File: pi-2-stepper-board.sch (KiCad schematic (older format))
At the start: 18 parts, among them CON1 DC12v, P1 Servo (A0), P2 Endstop1 (A1), P3 Endstop2 (A2), P4 Stepper1, P5 Stepper2, P6 COM, P7 Aux (D10 - 13), SW1 SW_PUSH, SW2 SPDT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

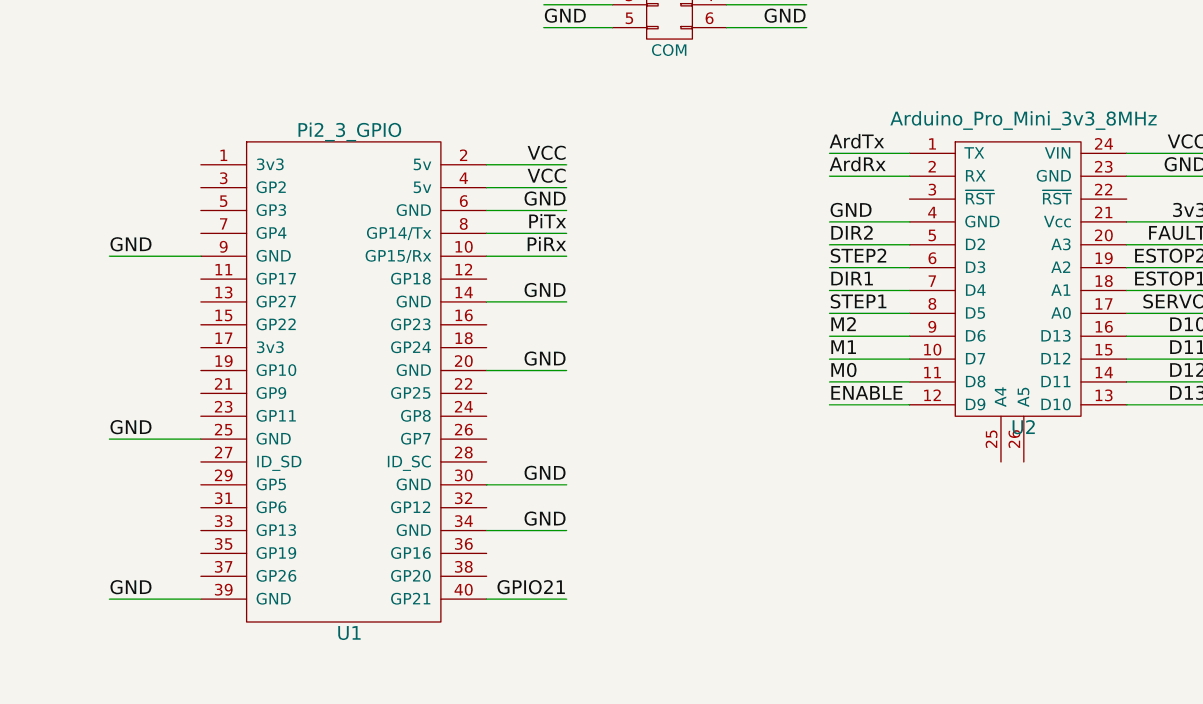
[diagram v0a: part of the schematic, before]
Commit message: Added I2C updated text
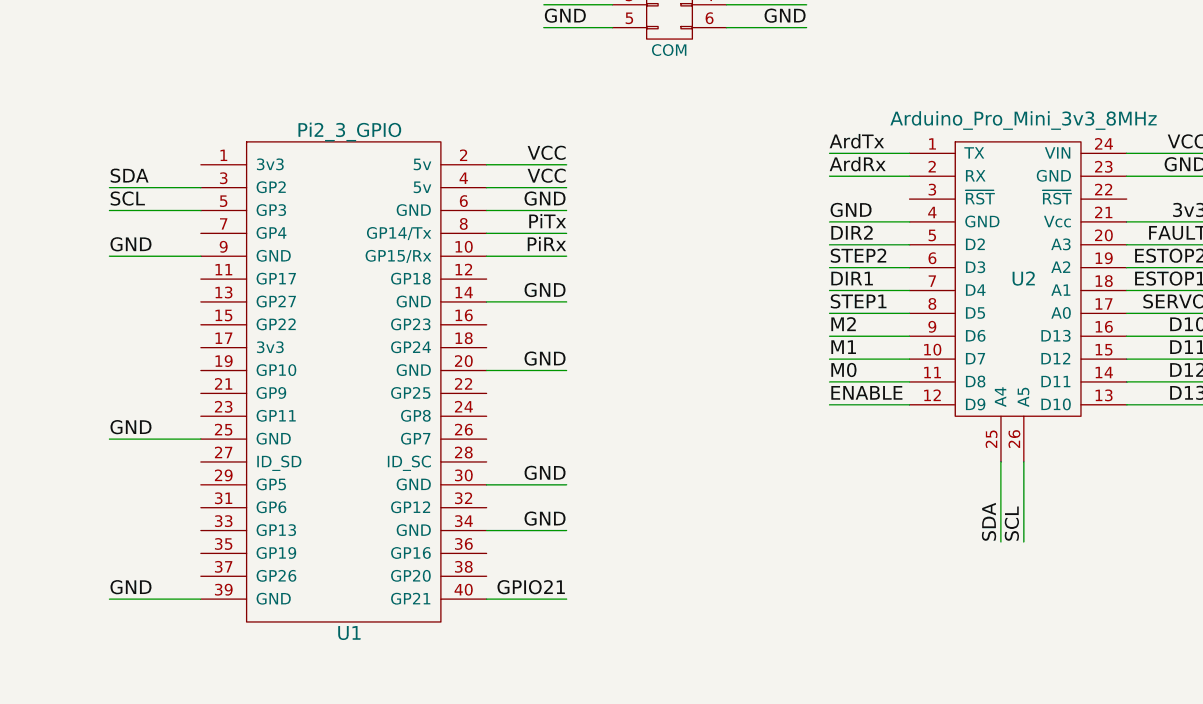
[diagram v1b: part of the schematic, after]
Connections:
- net SDA: now reaches U2.25 (A4)
- net SDA: now also U1.3 (GP2)
- net SCL: now reaches U2.26 (A5)
- net SCL: now also U1.5 (GP3)
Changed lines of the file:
@@
-$EndComp
-$Comp
-L Arduino_Pro_Mini_3v3_8MHz U2
-U 1 1 56E571C7
-P 5200 3050
-F 0 "U2" H 5200 2400 60  0000 C CNN
-F 1 "Arduino_Pro_Mini_3v3_8MHz" H 5200 3750 60  0000 C CNN
-F 2 "custom:Arduino_Pro_Mini" H 5200 2500 60  0001 C CNN
-F 3 "" H 5200 2500 60  0000 C CNN
-	1    5200 3050
-	1    0    0    -1
 $EndComp
 $Comp
@@
 	1    0    0    -1
 $EndComp
+$Comp
+L Arduino_Pro_Mini_3v3_8MHz U2
+U 1 1 56E88F52
+P 5200 3050
+F 0 "U2" H 5200 3050 60  0000 C CNN
+F 1 "Arduino_Pro_Mini_3v3_8MHz" H 5200 3750 60  0000 C CNN
+F 2 "custom:Arduino_Pro_Mini" H 5200 2500 60  0001 C CNN
+F 3 "" H 5200 2500 60  0000 C CNN
+	1    5200 3050
+	1    0    0    -1
+$EndComp
+Wire Wire Line
+	5100 3850 5100 4200
+Wire Wire Line
+	5200 3850 5200 4200
+Text Label 5100 4200 1    60   ~ 0
+SDA
+Text Label 5200 4200 1    60   ~ 0
+SCL
+Wire Wire Line
+	1600 2650 1200 2650
+Wire Wire Line
+	1600 2750 1200 2750
+Text Label 1200 2650 0    60   ~ 0
+SDA
+Text Label 1200 2750 0    60   ~ 0
+SCL
 $EndSCHEMATC

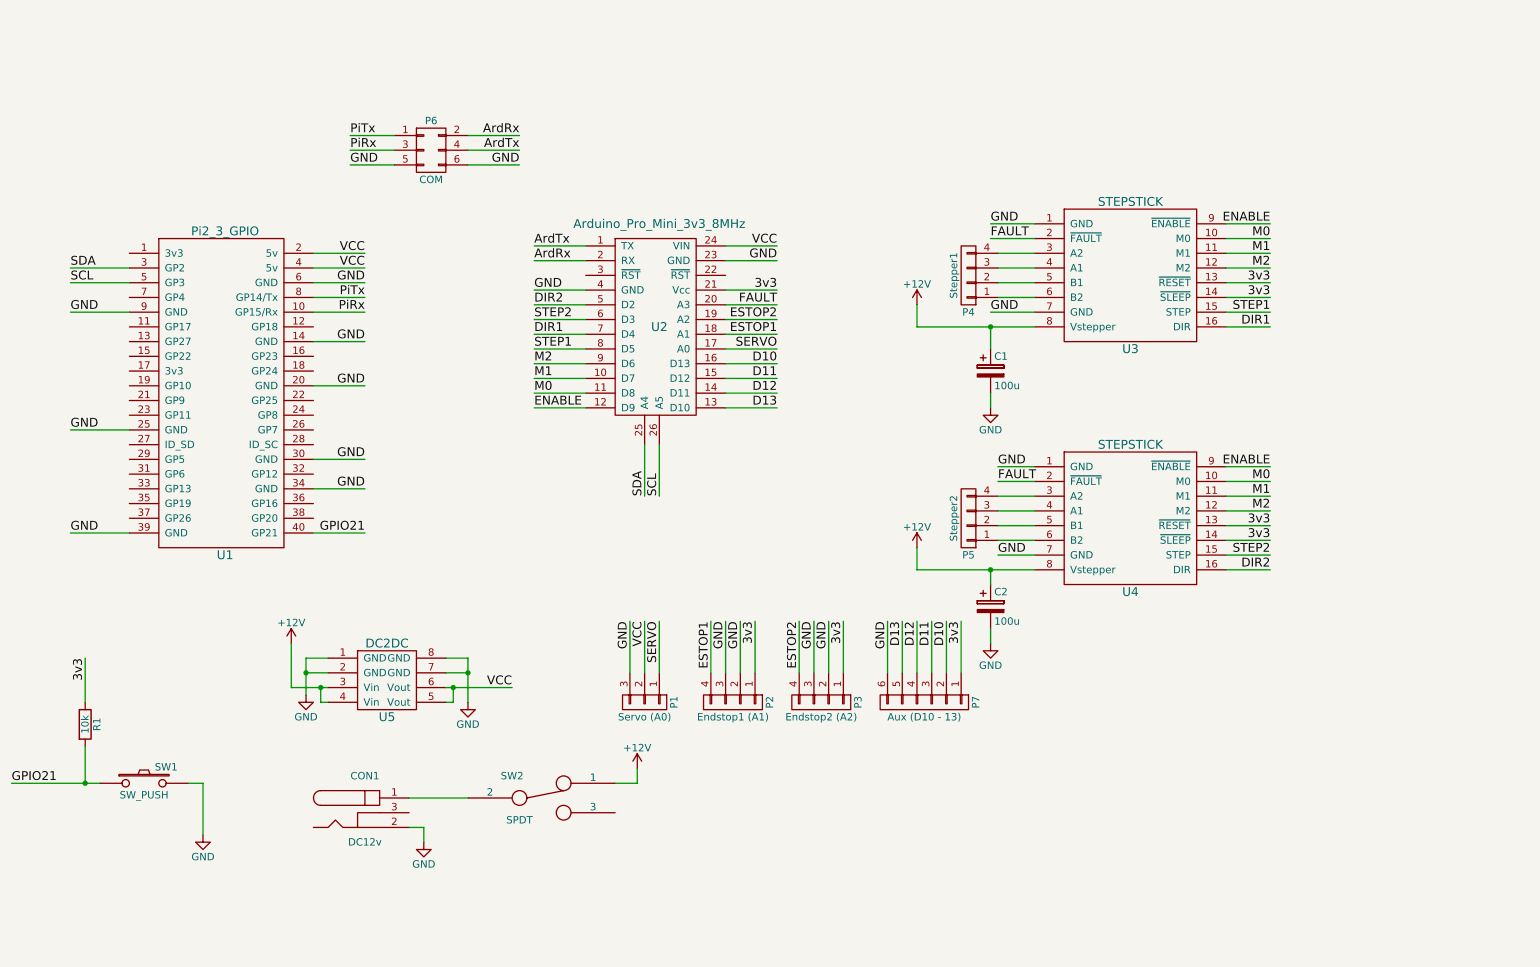
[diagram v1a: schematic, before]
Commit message: Added I2C port and other fixes
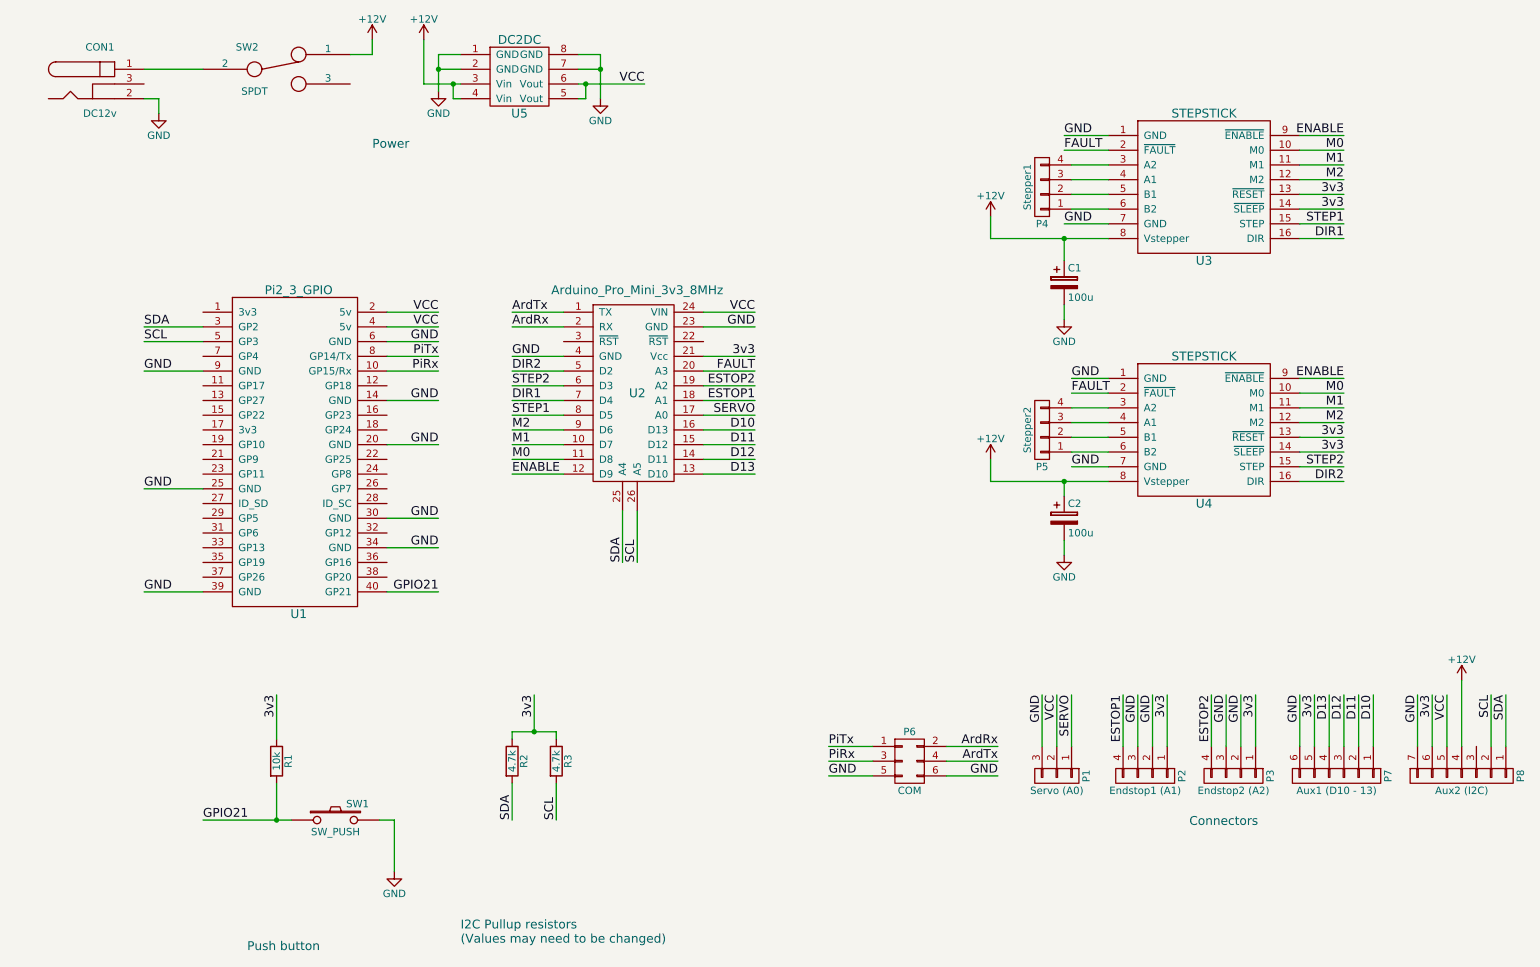
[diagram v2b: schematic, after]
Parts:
- added P8: Aux2 (I2C), Pin_Headers:Pin_Header_Straight_1x07, symbol CONN_01X07
- added R2, R3: 4.7k, Discret:R1, symbol R
- P7: value Aux (D10 - 13) -> Aux1 (D10 - 13); footprint Pin_Headers:Pin_Header_Straight_1x06 -> Pin_Headers:Pin_Header_Straight_1x07
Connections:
- net +12V: now also P8.4 (P4)
- net 3v3: now also P7.5 (P5), P8.6 (P6), R2.1, R3.1; no longer P7.1 (P1)
- net D10: now also P7.1 (P1); no longer P7.2 (P2)
- net D11: now also P7.2 (P2); no longer P7.3 (P3)
- net D12: now also P7.3 (P3); no longer P7.4 (P4)
- net D13: now also P7.4 (P4); no longer P7.5 (P5)
- net GND: now also P8.7 (P7)
- net SCL: now also P8.2 (P2), R3.2
- net SDA: now also P8.1 (P1), R2.2
- net VCC: now also P8.5 (P5)
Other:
- note added: "Connectors"
- note added: "I2C Pullup resistors \n(Values may need to be changed)"
- note added: "Power"
- note added: "Push button"
- moved on the sheet: C1, C2, CON1, P1, P2, P3, P4, P5, P6, P7, R1, SW1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
